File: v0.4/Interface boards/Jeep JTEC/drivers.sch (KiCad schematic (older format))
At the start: 12 parts, among them Q3 IRF540NPBF, Q4 IRF540NPBF, Q5 IRF540NPBF, Q6 IRF540NPBF, Q7 IRF540NPBF, Q8 IRF540NPBF

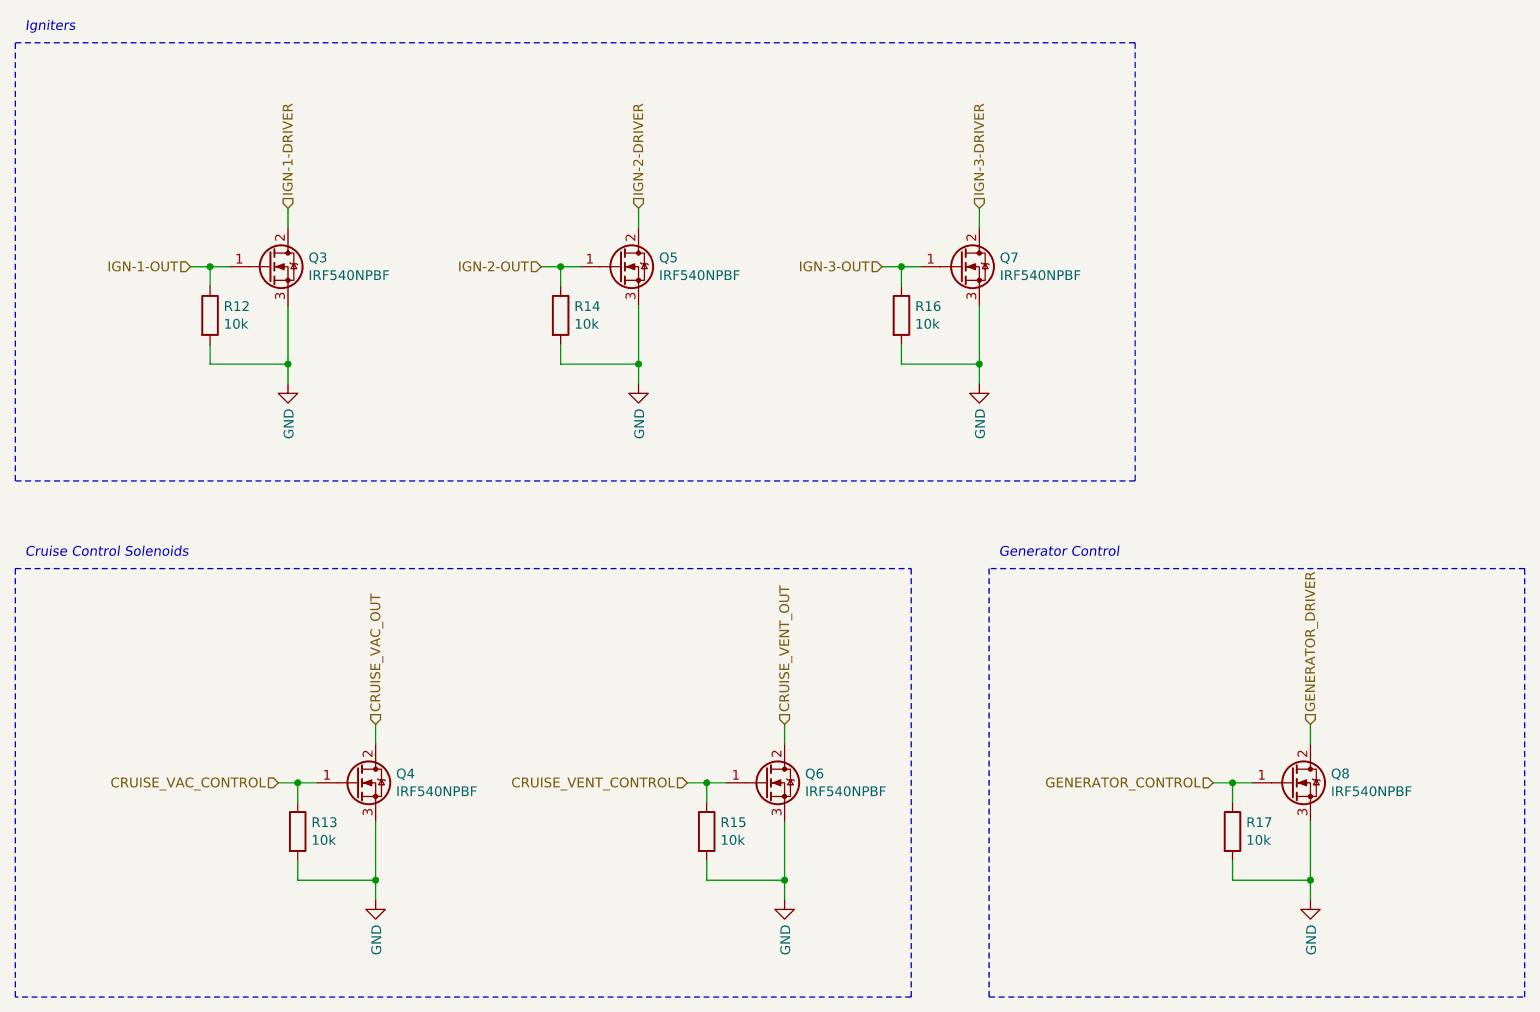
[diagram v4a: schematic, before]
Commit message: Add diodes to igniter circuit to allow ringing
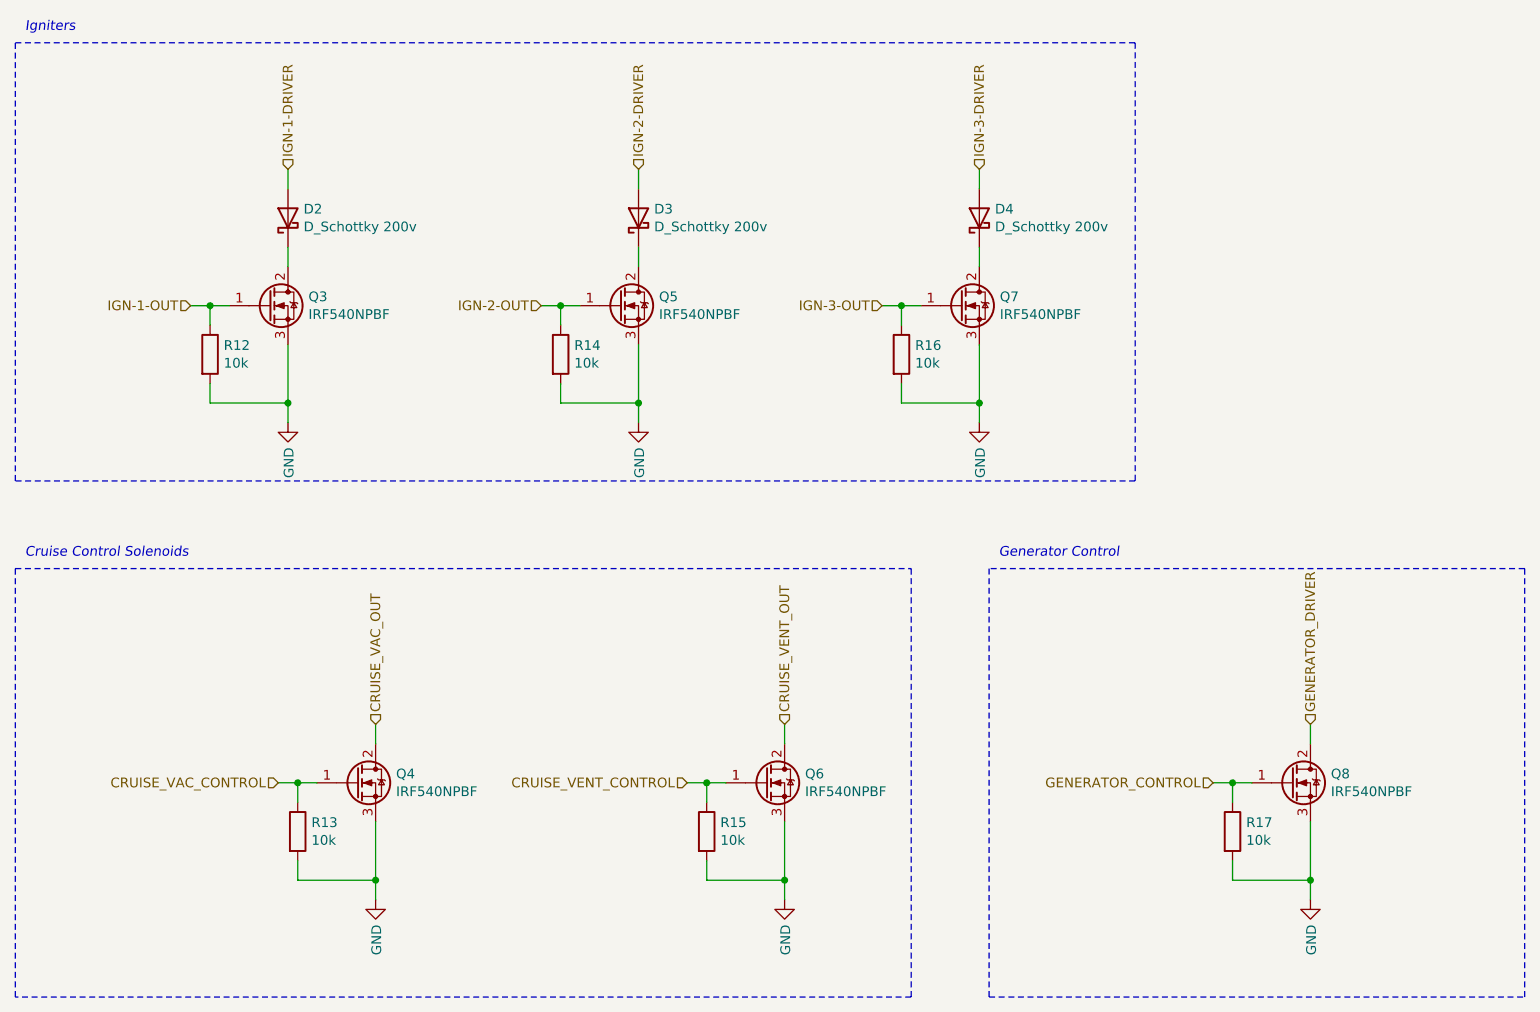
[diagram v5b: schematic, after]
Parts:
- added D2, D3, D4: D_Schottky 200v, Diode_SMD:D_SMB, symbol Device:D_Schottky
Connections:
- net IGN-1-DRIVER: now also D2.2 (A); no longer Q3.2 (D)
- net IGN-2-DRIVER: now also D3.2 (A); no longer Q5.2 (D)
- net IGN-3-DRIVER: now also D4.2 (A); no longer Q7.2 (D)
- new net: D2.1 (K), Q3.2 (D)
- new net: D3.1 (K), Q5.2 (D)
- new net: D4.1 (K), Q7.2 (D)
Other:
- moved on the sheet: Q3, Q5, Q7, R12, R14, R16
